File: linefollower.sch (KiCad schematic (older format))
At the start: 101 parts, among them J1 BATT, J10 LINE_SENS, J11 I2C, J12 BT_module, J13 USB_B_Micro, J14 Micro_SD_Card_Det, J2 ESC, J3 ESC_CTRL, J4 3v3, J5 3v3, J6 5v, J7 SWD+UART, J8 SPI2, J9 I2C, SW2 SW0, SW3 SW1, SW4 SW2, SW5 SW3, SW6 SW_DIP_x04, SW7 RST, U1 MAX14870_carrier, U10 ADG726BSUZ, U11 HC-05, U12 IP4220CZ6, U13 STM32F429ZITx, U2 MAX14870_carrier, U3 L7805, U4 LM1117-3.3, U5 M_R, U6 M_L, U7 Troyka-IMU10, U8 AltIMU-10v5, U9 UM7, Y1 8MHz, Y2 32MHz

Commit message: PDF added
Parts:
- U1: footprint Crystal:Crystal_SMD_3215-2Pin_3.2x1.5mm -> Module:MAX14870_carrier_board
- U2: footprint (none) -> Module:MAX14870_carrier_board
- U5, U6: footprint (none) -> Connector_JST:JST_SH_BM06B-SRSS-TB_1x06-1MP_P1.00mm_Vertical
- U8: footprint (none) -> Sensor_Motion:AltIMUv10
- U9: footprint (none) -> Connector_JST:JST_SH_BM05B-SRSS-TB_1x05-1MP_P1.00mm_Vertical
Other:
- moved on the sheet: C1, C10, C11, C12, C13, C14, C15, C16, C17, C18, C19, C2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

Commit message: Added voltage & current sensing; Minor fixes
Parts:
- removed C9: 100nF, Capacitor_SMD:C_0805_2012Metric, symbol Device:C_Small
- removed D1: stps2l40u, Diode_SMD:D_SMB, symbol Device:D_Schottky_Small
- removed D9: LED, LED_SMD:LED_0603_1608Metric, symbol Device:LED
- removed J12: BT_module, Connector_PinSocket_2.54mm:PinSocket_1x04_P2.54mm_Vertical, symbol Connector_Generic:Conn_01x04
- removed R19: 300r, Resistor_SMD:R_0805_2012Metric, symbol Device:R_Small
- removed U11: HC-05, bt-hc-05:HC-05, symbol linefollower-rescue:HC-05-HC_05
- added C3: 1nF, Capacitor_SMD:C_0805_2012Metric, symbol Device:C_Small
- added C34: 1uF, Capacitor_SMD:C_0805_2012Metric, symbol Device:C_Small
- added C35, C36: 100uF, Capacitor_SMD:CP_Elec_6.3x5.4, symbol Device:CP1_Small
- added C4: 100nF, Capacitor_SMD:C_0805_2012Metric, symbol Device:C_Small
- added J11: BT_module, Connector_PinSocket_2.54mm:PinSocket_1x04_P2.54mm_Vertical, symbol Connector_Generic:Conn_01x04
- added R10: 5.6k, Resistor_SMD:R_0805_2012Metric, symbol Device:R_Small
- added R25: 47k, Resistor_SMD:R_0805_2012Metric, symbol Device:R_Small
- added R6: 1k, Resistor_SMD:R_0805_2012Metric, symbol Device:R_Small
- added R7: 1.8k, Resistor_SMD:R_0805_2012Metric, symbol Device:R_Small
- added R9: 20k, Resistor_SMD:R_0805_2012Metric, symbol Device:R_Small
- added U1: ACS712xLCTR-30A, Package_SO:SOIC-8_3.9x4.9mm_P1.27mm, symbol Sensor_Current:ACS712xLCTR-30A
- J1: footprint (none) -> Connector:Soldered_pad_4x6_01x02
- J8: renamed from J2; footprint (none) -> Connector:Soldered_pad_4x6_01x02
- JP1: footprint (none) -> Jumper:SolderJumper-3_P1.3mm_Open_RoundedPad1.0x1.5mm
- SW1: renamed from SW2; value SW0 -> uBTN_0
- SW2: renamed from SW3; value SW1 -> uBTN_1
- SW3: renamed from SW4; value SW2 -> uBTN_2
- SW4: renamed from SW5; value SW3 -> uBTN_3
- U10: renamed from U7; footprint (none) -> Sensor_Motion:Troyka_IMU
- renumbered C8 to C10, C10 to C11, C11 to C12, C12 to C13, C13 to C14, C14 to C15, C15 to C16, C16 to C17, C17 to C18, C18 to C19, C19 to C20, C20 to C21, C21 to C22, C22 to C23, C23 to C24, C24 to C25, C25 to C26, C28 to C27, C29 to C28, C30 to C29, C31 to C30, C32 to C31, C26 to C32, C27 to C33, C3 to C5, C4 to C6, C5 to C7, C6 to C8, C7 to C9, D4 to D1, D5 to D2, D2 to D3, D3 to D4, D6 to D5, D7 to D6, D8 to D7, J11 to J10, J13 to J12, J10 to J13, J4 to J2, J5 to J3, J6 to J4, J7 to J5, J8 to J6, J9 to J7, J3 to J9, R3 to R1, R9 to R11, R10 to R12, R11 to R13, R12 to R14, R13 to R15, R14 to R16, R15 to R17, R16 to R18, R1 to R19, R4 to R2, R2 to R20, R17 to R21, R18 to R22, R20 to R23, R21 to R24, R5 to R3, R6 to R4, R7 to R5, SW6 to SW5, SW7 to SW6, U8 to U11, U9 to U12, U3 to U2, U4 to U3, U12 to U4, U1 to U5, U2 to U6, U10 to U7, U5 to U8, U6 to U9
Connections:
- net +12V: now also F1.2
- net +3V3: now also J11.4 (Pin_4)
- net +5V: now also C2.1, C6.1, D4.1 (K), JP2.2, U3.3 (VI), C4.2, U1.8 (VCC); no longer JP2.1
- net +BATT: now also R9.1, U1.3 (IP-), U1.4 (IP-); no longer J1.2 (Pin_2)
- net GND: now also C3.2, C34.2, C35.2, C36.2, C4.1, J11.3 (Pin_3), R10.2, R7.2, U1.5 (GND)
- net UART6_RX: now also J11.2 (Pin_2)
- net UART6_TX: now also J11.1 (Pin_1)
- net VBUS: now also JP2.1; no longer C2.1, C6.1, D4.1 (K), JP2.2, U3.3 (VI)
- net CURR_SENS: now reaches U13.21 (PF9)
- net CURR_SENS: now also C34.1, R25.1
- net VOLT_SENS: now reaches U13.22 (PF10)
- net VOLT_SENS: now also R10.1, R9.2
- new net: C35.1, C36.1, J1.2 (Pin_2), U1.1 (IP+), U1.2 (IP+)
- new net: C3.1, U1.6 (FILTER)
- new net: R6.1, U1.7 (VIOUT)
- new net: R25.2, R6.2, R7.1
- no-connect marks 101 -> 72
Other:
- moved on the sheet: C1, C10, C11, C12, C13, C14, C15, C16, C17, C18, C19, C2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

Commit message: Fixed footprints
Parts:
- U10: footprint Sensor_Motion:Troyka_IMU -> linefollower:Troyka_IMU
- U11: footprint Sensor_Motion:AltIMUv10 -> linefollower:AltIMU10_v5
- U5, U6: footprint Module:MAX14870_carrier_board -> linefollower:MAX14870_Carrier
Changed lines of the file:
@@
 F 0 "U6" H 8075 4565 50  0000 C CNN
 F 1 "MAX14870_carrier" H 8075 4474 50  0000 C CNN
-F 2 "Module:MAX14870_carrier_board" H 8050 4550 50  0001 C CNN
+F 2 "linefollower:MAX14870_Carrier" H 8050 4550 50  0001 C CNN
 F 3 "" H 8050 4550 50  0001 C CNN
 	1    8050 4550
@@
 F 0 "U5" H 8050 5715 50  0000 C CNN
 F 1 "MAX14870_carrier" H 8050 5624 50  0000 C CNN
-F 2 "Module:MAX14870_carrier_board" H 8025 5700 50  0001 C CNN
+F 2 "linefollower:MAX14870_Carrier" H 8025 5700 50  0001 C CNN
 F 3 "" H 8025 5700 50  0001 C CNN
 	1    8025 5700
@@
 F 0 "U11" H 10450 9300 50  0000 L CNN
 F 1 "AltIMU-10v5" H 10250 9200 50  0000 L CNN
-F 2 "Sensor_Motion:AltIMUv10" H 10475 9175 50  0001 C CNN
+F 2 "linefollower:AltIMU10_v5" H 10475 9175 50  0001 C CNN
 F 3 "" H 10475 9175 50  0001 C CNN
 	1    10675 8525
@@
 F 0 "U10" H 10500 9465 50  0000 C CNN
 F 1 "Troyka-IMU10" H 10500 9374 50  0000 C CNN
-F 2 "Sensor_Motion:Troyka_IMU" H 10300 9450 50  0001 C CNN
+F 2 "linefollower:Troyka_IMU" H 10300 9450 50  0001 C CNN
 F 3 "" H 10300 9450 50  0001 C CNN
 	1    10300 9450

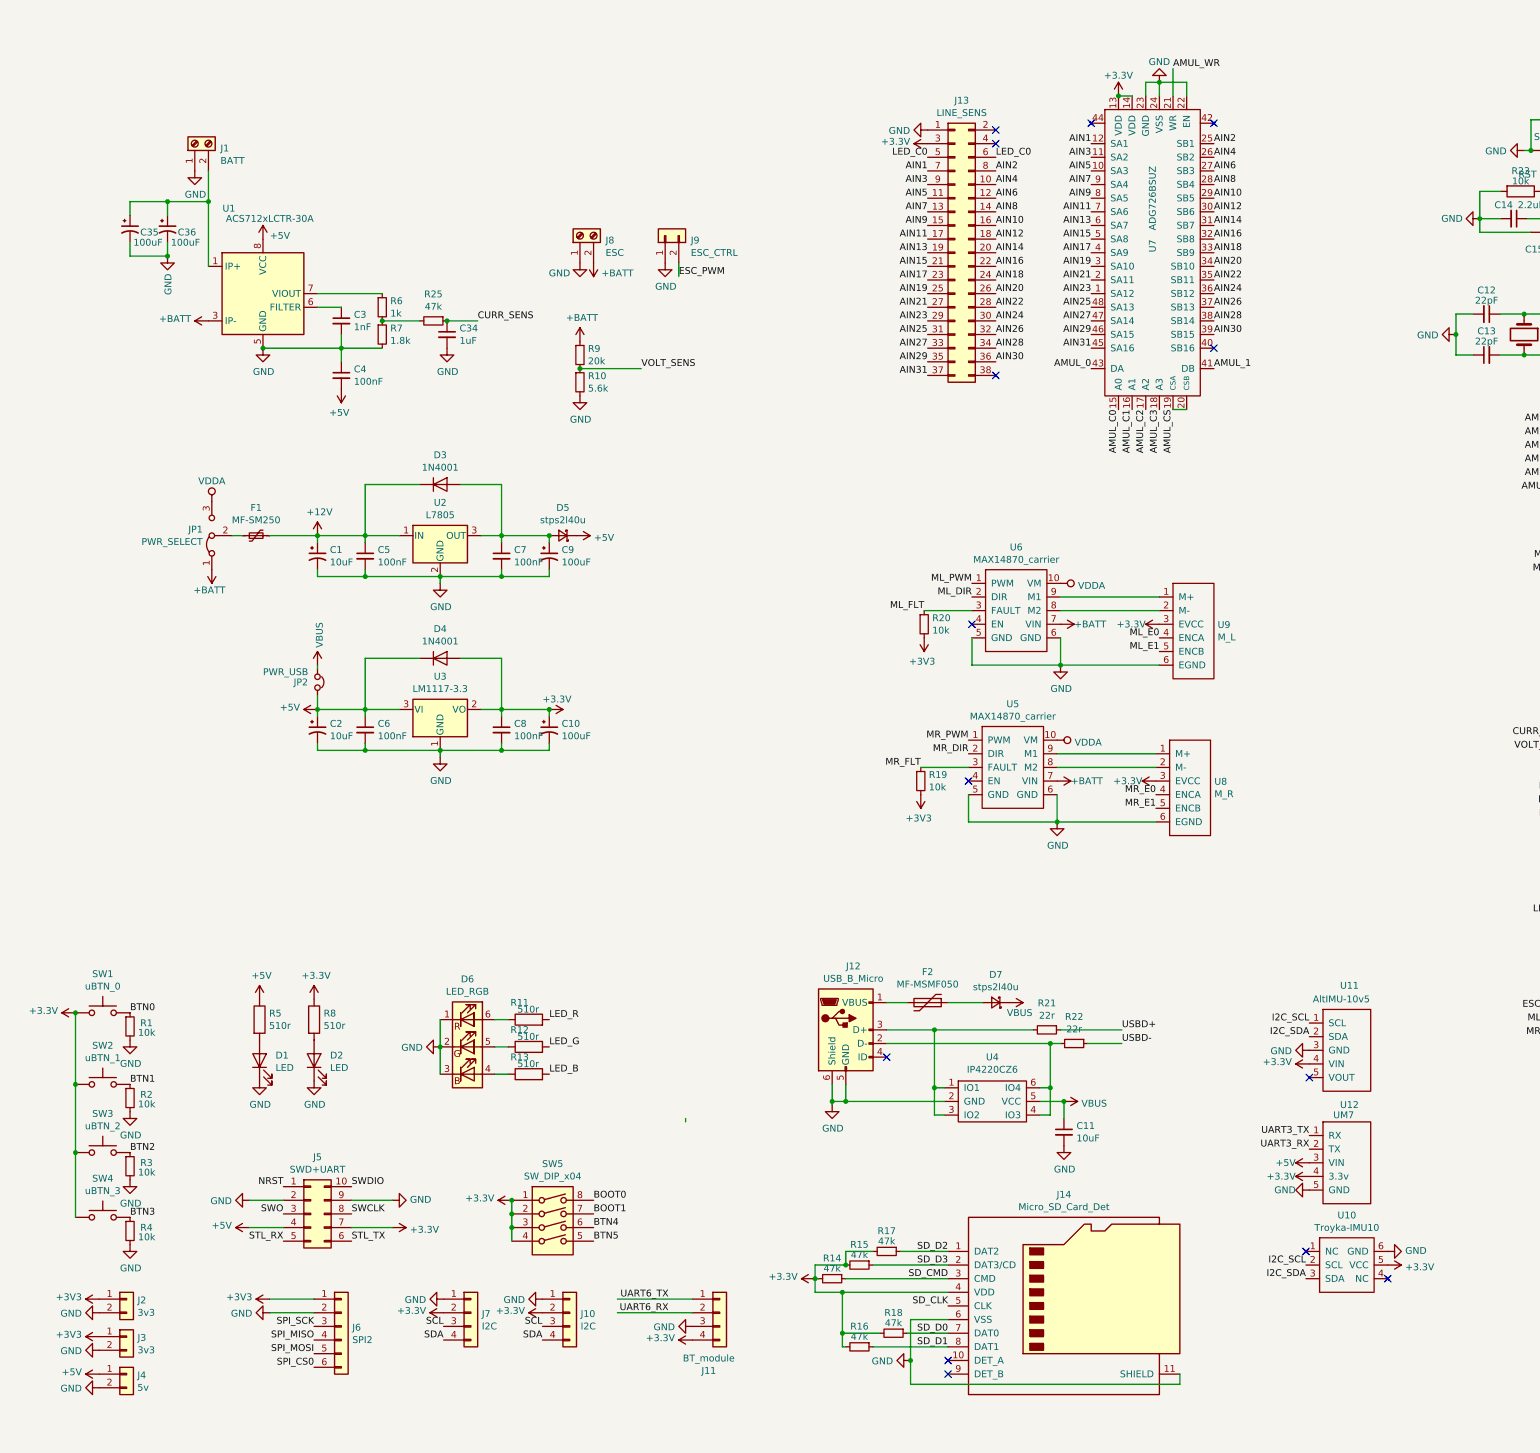
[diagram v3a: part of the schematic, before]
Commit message: Minor schematic fixes - now RC; Basic PCB
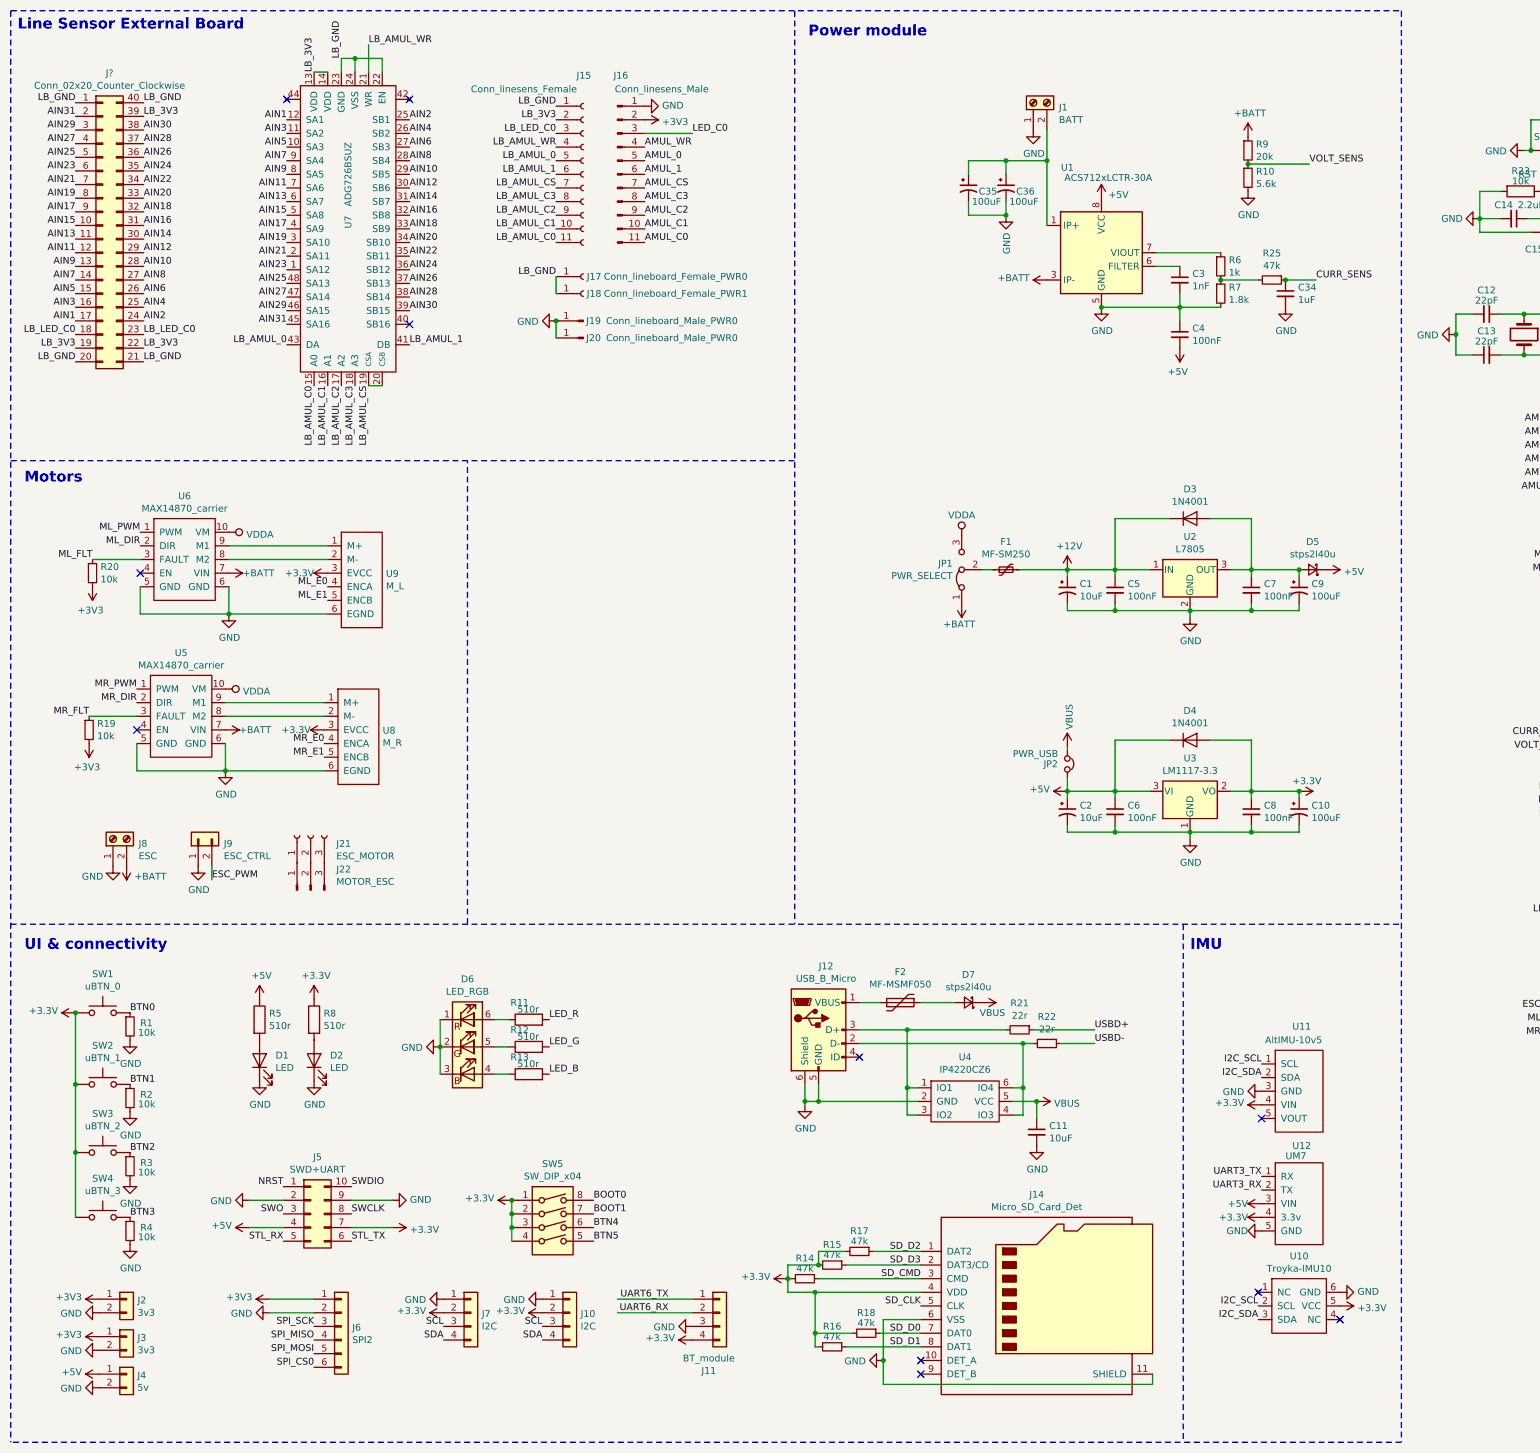
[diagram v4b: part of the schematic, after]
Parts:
- removed J13: LINE_SENS, Connector_PinHeader_2.54mm:PinHeader_2x19_P2.54mm_Vertical, symbol Connector_Generic:Conn_02x19_Odd_Even
- added J15: Conn_linesens_Female, Connector_PinSocket_2.54mm:PinSocket_1x11_P2.54mm_Horizontal, symbol Connector:Conn_01x11_Female
- added J16: Conn_linesens_Male, Connector_PinSocket_2.54mm:PinSocket_1x11_P2.54mm_Horizontal, symbol Connector:Conn_01x11_Male
- added J17: Conn_lineboard_Female_PWR0, linefollower:Soldered_pad_01x01_4x6, symbol Connector:Conn_01x01_Female
- added J18: Conn_lineboard_Female_PWR1, linefollower:Soldered_pad_01x01_4x6, symbol Connector:Conn_01x01_Female
- added J19, J20: Conn_lineboard_Male_PWR0, linefollower:Soldered_pad_01x01_4x6, symbol Connector:Conn_01x01_Male
- added J21: ESC_MOTOR, linefollower:Soldered_pad_01x03_4x5, symbol Connector:Conn_01x03_Female
- added J22: MOTOR_ESC, linefollower:Soldered_pad_01x03_4x5, symbol Connector:Conn_01x03_Male
- added J?: Conn_02x20_Counter_Clockwise, symbol Connector_Generic:Conn_02x20_Counter_Clockwise
- F1: footprint Fuse:Fuse_Bourns_MF-SM_9.5x6.71mm -> linefollower:MF-MSMF-A
- F2: footprint Fuse:MF-MSMF -> linefollower:MF-MSMF-A
- J1, J8: footprint Connector:Soldered_pad_4x6_01x02 -> linefollower:Soldered_pad_01x02_4x6
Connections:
- net +3V3: now also J16.2 (Pin_2); no longer U7.13 (VDD), U7.14 (VDD)
- net AIN1: now also J?.17 (Pin_17)
- net AIN10: now also J?.28 (Pin_28)
- net AIN11: now also J?.12 (Pin_12)
- net AIN12: now also J?.29 (Pin_29)
- net AIN13: now also J?.11 (Pin_11)
- net AIN14: now also J?.30 (Pin_30)
- net AIN15: now also J?.10 (Pin_10)
- net AIN16: now also J?.31 (Pin_31)
- net AIN17: now also J?.9 (Pin_9)
- net AIN18: now also J?.32 (Pin_32)
- net AIN19: now also J?.8 (Pin_8)
- net AIN2: now also J?.24 (Pin_24)
- net AIN20: now also J?.33 (Pin_33)
- net AIN21: now also J?.7 (Pin_7)
- net AIN22: now also J?.34 (Pin_34)
- net AIN23: now also J?.6 (Pin_6)
- net AIN24: now also J?.35 (Pin_35)
- net AIN25: now also J?.5 (Pin_5)
- net AIN26: now also J?.36 (Pin_36)
- net AIN27: now also J?.4 (Pin_4)
- net AIN28: now also J?.37 (Pin_37)
- net AIN29: now also J?.3 (Pin_3)
- net AIN3: now also J?.16 (Pin_16)
- net AIN30: now also J?.38 (Pin_38)
- net AIN31: now also J?.2 (Pin_2)
- net AIN4: now also J?.25 (Pin_25)
- net AIN5: now also J?.15 (Pin_15)
- net AIN6: now also J?.26 (Pin_26)
- net AIN7: now also J?.14 (Pin_14)
- net AIN8: now also J?.27 (Pin_27)
- net AIN9: now also J?.13 (Pin_13)
- net AMUL_0: now also J16.5 (Pin_5); no longer U7.43 (DA)
- net AMUL_1: now also J16.6 (Pin_6); no longer U7.41 (DB)
- net AMUL_C0: now also J16.11 (Pin_11); no longer U7.15 (A0)
- net AMUL_C1: now also J16.10 (Pin_10); no longer U7.16 (A1)
- net AMUL_C2: now also J16.9 (Pin_9); no longer U7.17 (A2)
- net AMUL_C3: now also J16.8 (Pin_8); no longer U7.18 (A3)
- net AMUL_CS: now also J16.7 (Pin_7); no longer U7.19 (CSA), U7.20 (CSB)
- net AMUL_WR: now also J16.4 (Pin_4); no longer U7.21 (WR)
- net GND: now also J16.1 (Pin_1), J19.1 (Pin_1), J20.1 (Pin_1); no longer U7.22 (EN), U7.23 (GND), U7.24 (VSS)
- net LED_C0: now also J16.3 (Pin_3)
- new net: J21.1 (Pin_1), J22.1 (Pin_1)
- new net: J21.2 (Pin_2), J22.2 (Pin_2)
- new net: J21.3 (Pin_3), J22.3 (Pin_3)
- new net LB_3V3: J15.2 (Pin_2), J?.19 (Pin_19), J?.22 (Pin_22), J?.39 (Pin_39), U7.13 (VDD), U7.14 (VDD)
- new net LB_AMUL_0: J15.5 (Pin_5), U7.43 (DA)
- new net LB_AMUL_1: J15.6 (Pin_6), U7.41 (DB)
- new net LB_AMUL_C0: J15.11 (Pin_11), U7.15 (A0)
- new net LB_AMUL_C1: J15.10 (Pin_10), U7.16 (A1)
- new net LB_AMUL_C2: J15.9 (Pin_9), U7.17 (A2)
- new net LB_AMUL_C3: J15.8 (Pin_8), U7.18 (A3)
- new net LB_AMUL_CS: J15.7 (Pin_7), U7.19 (CSA), U7.20 (CSB)
- new net LB_AMUL_WR: J15.4 (Pin_4), U7.21 (WR)
- new net LB_GND: J15.1 (Pin_1), J17.1 (Pin_1), J18.1 (Pin_1), J?.1 (Pin_1), J?.20 (Pin_20), J?.21 (Pin_21), J?.40 (Pin_40), U7.22 (EN), U7.23 (GND), U7.24 (VSS)
- new net LB_LED_C0: J15.3 (Pin_3), J?.18 (Pin_18), J?.23 (Pin_23)
- no-connect marks 72 -> 69
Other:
- note added: "IMU"
- note added: "Line Sensor External Board"
- note added: "Motors\n\n"
- note added: "Power module\n"
- note added: "UI & connectivity"
- moved on the sheet: C1, C10, C11, C2, C3, C34, C35, C36, C4, C5, C6, C7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

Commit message: PCB for linesensor board and powermodule finished
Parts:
- removed C11: 10uF, Capacitor_SMD:CP_Elec_5x5.3, symbol Device:C_Small
- removed J17: Conn_lineboard_Female_PWR0, linefollower:Soldered_pad_01x01_4x6, symbol Connector:Conn_01x01_Female
- removed J18: Conn_lineboard_Female_PWR1, linefollower:Soldered_pad_01x01_4x6, symbol Connector:Conn_01x01_Female
- removed J19, J20: Conn_lineboard_Male_PWR0, linefollower:Soldered_pad_01x01_4x6, symbol Connector:Conn_01x01_Male
- removed J?: Conn_02x20_Counter_Clockwise, symbol Connector_Generic:Conn_02x20_Counter_Clockwise
- added C37, C38: 100nF, Capacitor_SMD:C_0805_2012Metric, symbol Device:C_Small
- added D10, D8, D9: LED, LED_SMD:LED_0603_1608Metric, symbol Device:LED
- added J13: Conn_02x20_Odd_Even, Connector_PinSocket_2.54mm:PinSocket_2x20_P2.54mm_Vertical, symbol Connector_Generic:Conn_02x20_Odd_Even
- added R26, R27, R28: 510r, Resistor_SMD:R_0805_2012Metric, symbol Device:R
- J15: footprint Connector_PinSocket_2.54mm:PinSocket_1x11_P2.54mm_Horizontal -> linefollower:SolderedPad_1x11_P2.54
- JP2: footprint Connector_PinSocket_2.54mm:PinSocket_1x02_P2.54mm_Vertical -> Jumper:SolderJumper-2_P1.3mm_Open_RoundedPad1.0x1.5mm
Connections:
- net AIN1: now also J13.33 (Pin_33)
- net AIN10: now also J13.26 (Pin_26)
- net AIN11: now also J13.23 (Pin_23)
- net AIN12: now also J13.24 (Pin_24)
- net AIN13: now also J13.21 (Pin_21)
- net AIN14: now also J13.22 (Pin_22)
- net AIN15: now also J13.19 (Pin_19)
- net AIN16: now also J13.20 (Pin_20)
- net AIN17: now also J13.17 (Pin_17)
- net AIN18: now also J13.18 (Pin_18)
- net AIN19: now also J13.15 (Pin_15)
- net AIN2: now also J13.34 (Pin_34)
- net AIN20: now also J13.16 (Pin_16)
- net AIN21: now also J13.13 (Pin_13)
- net AIN22: now also J13.14 (Pin_14)
- net AIN23: now also J13.11 (Pin_11)
- net AIN24: now also J13.12 (Pin_12)
- net AIN25: now also J13.9 (Pin_9)
- net AIN26: now also J13.10 (Pin_10)
- net AIN27: now also J13.7 (Pin_7)
- net AIN28: now also J13.8 (Pin_8)
- net AIN29: now also J13.5 (Pin_5)
- net AIN3: now also J13.31 (Pin_31)
- net AIN30: now also J13.6 (Pin_6)
- net AIN31: now also J13.3 (Pin_3)
- net AIN4: now also J13.32 (Pin_32)
- net AIN5: now also J13.29 (Pin_29)
- net AIN6: now also J13.30 (Pin_30)
- net AIN7: now also J13.27 (Pin_27)
- net AIN8: now also J13.28 (Pin_28)
- net AIN9: now also J13.25 (Pin_25)
- net GND: now also C38.2, D10.1 (K)
- net LB_3V3: now also C37.1, J13.37 (Pin_37), J13.38 (Pin_38), J13.4 (Pin_4), R27.1
- net LB_AMUL_WR: now also R26.1
- net LB_GND: now also C37.2, D8.1 (K), D9.1 (K), J13.1 (Pin_1), J13.2 (Pin_2), J13.39 (Pin_39), J13.40 (Pin_40)
- net LB_LED_C0: now also J13.35 (Pin_35), J13.36 (Pin_36)
- net VBUS: now also R28.1
- net VOLT_SENS: now also C38.1
- new net: D9.2 (A), R27.2
- new net: D8.2 (A), R26.2
- new net: D10.2 (A), R28.2
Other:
- moved on the sheet: D1, D2, R5, R8

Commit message: MCU's main peripherals PCB
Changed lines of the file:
@@
 P 12050 1625
 F 0 "SW6" H 11950 1725 50  0000 C CNN
-F 1 " RST" H 11825 1450 50  0000 C CNN
+F 1 " RST" H 12025 1575 50  0000 C CNN
 F 2 "Button_Switch_SMD:SW_SPST_FSMSM" H 12050 1825 50  0001 C CNN
 F 3 "" H 12050 1825 50  0001 C CNN
